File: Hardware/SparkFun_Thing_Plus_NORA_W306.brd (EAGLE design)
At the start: 22.9 x 58.4 mm, 153 parts, among them J1 THING_PLUS_LOGICAL, J2 LiPo, J3 QWIIC_RA, J4 MICRO-SDFRICTION, J5 USB-C, J6 SWD (DNP), Q1 3.1A/30V/105mΩ, Q2 MBT3904DW1T1, U1 UBLOX_NORA_W306, U3 XC6222B331MR-G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

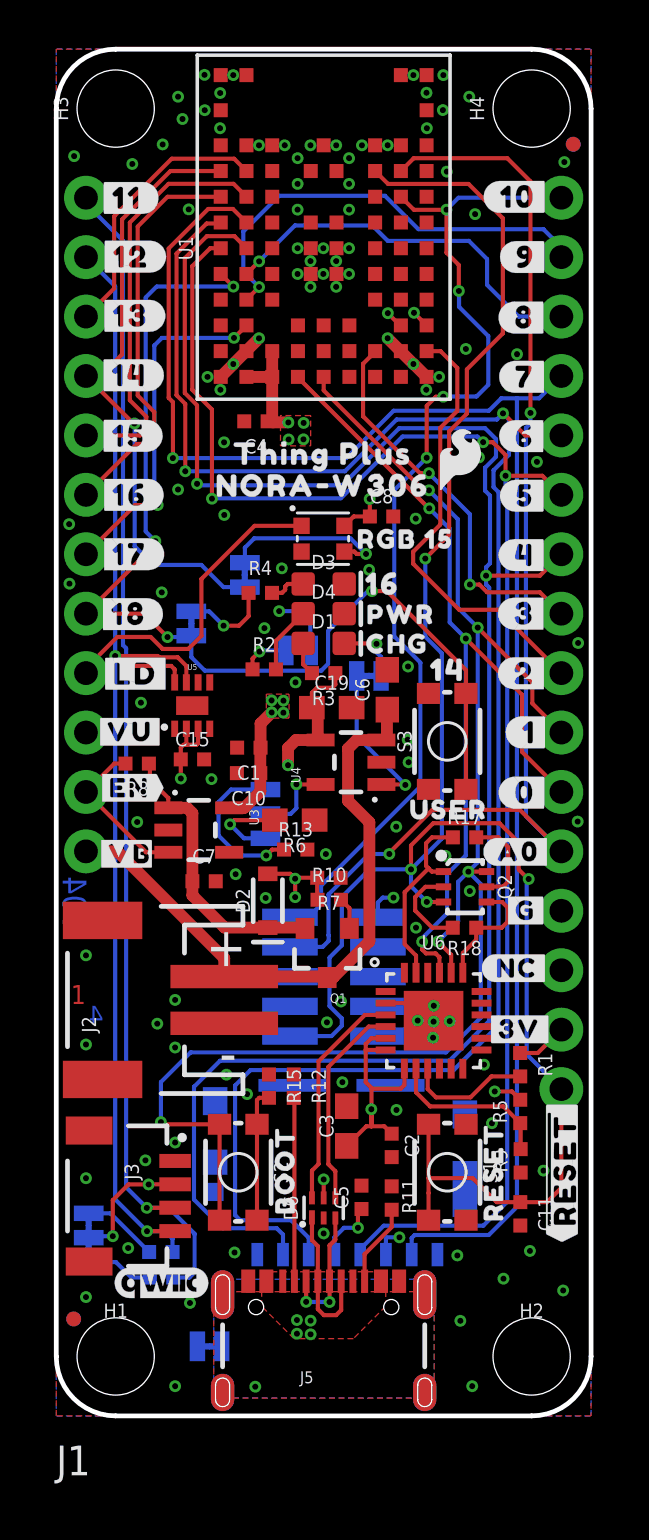
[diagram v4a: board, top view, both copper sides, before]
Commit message: Corrected User button and STAT LED silk
-Moved button to Arduino "17"
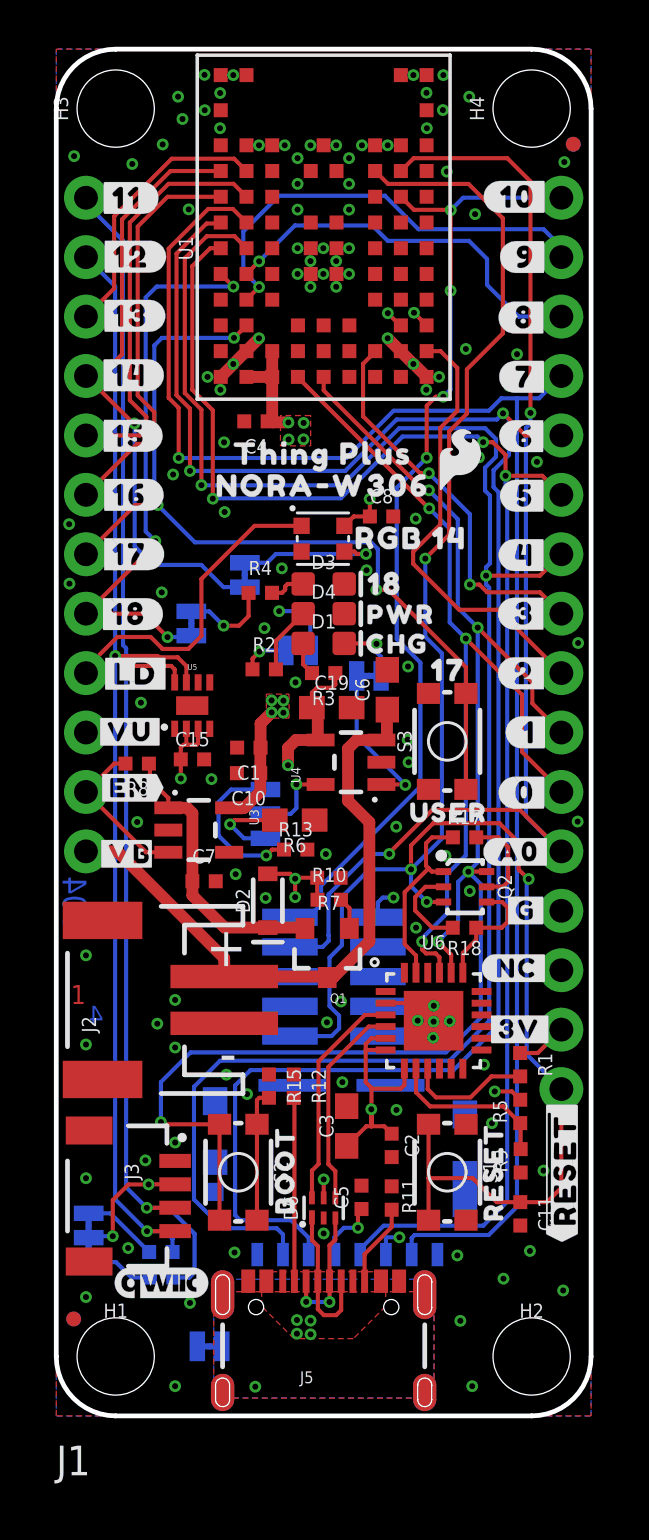
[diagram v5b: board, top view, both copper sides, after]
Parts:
- removed U$25: (no value), output:16165
- removed U$34: (no value), output:1417
- removed U$73: (no value), output:RGB_155
- added U$21: (no value), output:1830
- added U$22: (no value), output:1714141833
- added U$24: (no value), output:RGB_14141832
- moved U$7 0.13 mm to (16.8, 25.8)
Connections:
- net PB22: no longer S3.1, S3.2
- net PB23: now also S3.1, S3.2
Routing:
- net PB23: track 15.1 -> 37.5 mm, vias 2 -> 3
- net PB22: track 46.2 -> 24.6 mm, vias 4 -> 3
- net PA27/SWD_DATA: track 44.2 -> 41.9 mm
- net N$10: track 7.23 -> 6.30 mm

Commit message: rerouting some stuff
-Re-routed SPI lined to removed one via in SPI0_CLK net
-Nudged some stuff to create a bit more clearance between RX/TX log and SPI traces on long north-south journey.
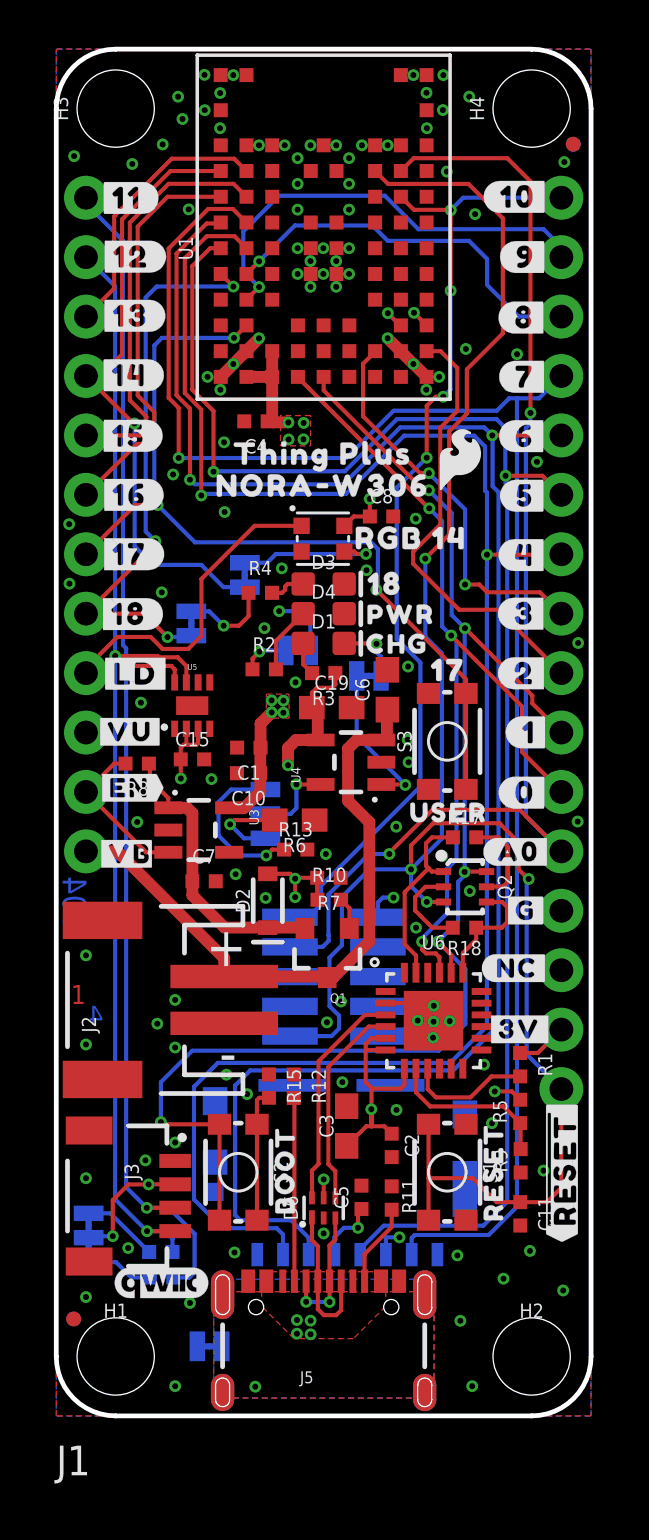
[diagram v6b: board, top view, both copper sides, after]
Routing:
- net PA7/UART-LOG-TXD: track 65.6 -> 62.3 mm
- net PB18/SPI0_PICO: track 78.0 -> 76.9 mm
- net PB21/SPI0_CS: track 79.8 -> 78.8 mm
- net PB20/SPI0_CLK: track 67.8 -> 67.4 mm, vias 3 -> 2
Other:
- board text added: "Soldermask: Red Thickness: 1.6mm Four Layer Design 1oz copper outer 0.5oz copper inner Finish: HASL Stackup: JLC7628 Material: TG155"
- board text removed: "Board thickness is 1.6mm 4-Layer 1oz copper outer 0.5oz copper inner Surface Finish: HASL"

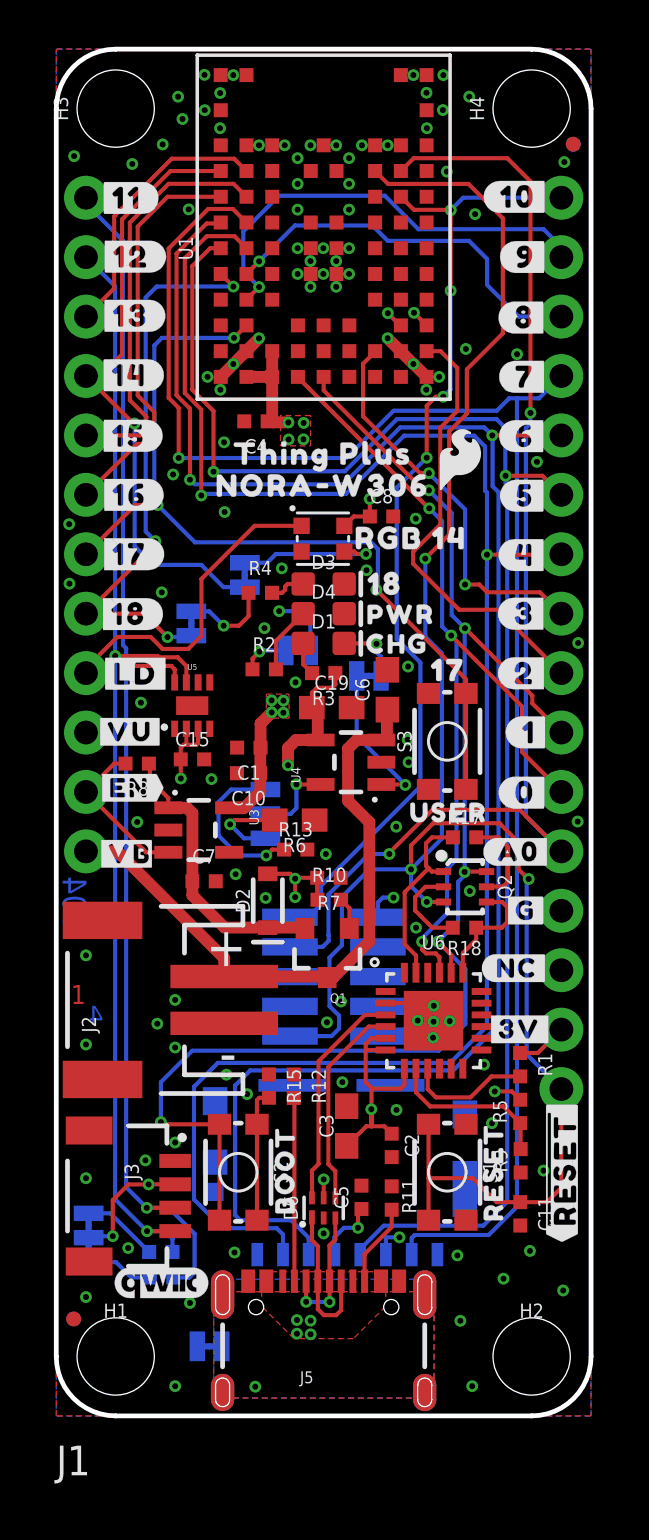
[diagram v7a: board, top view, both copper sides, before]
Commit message: Added V-MEAS jumper
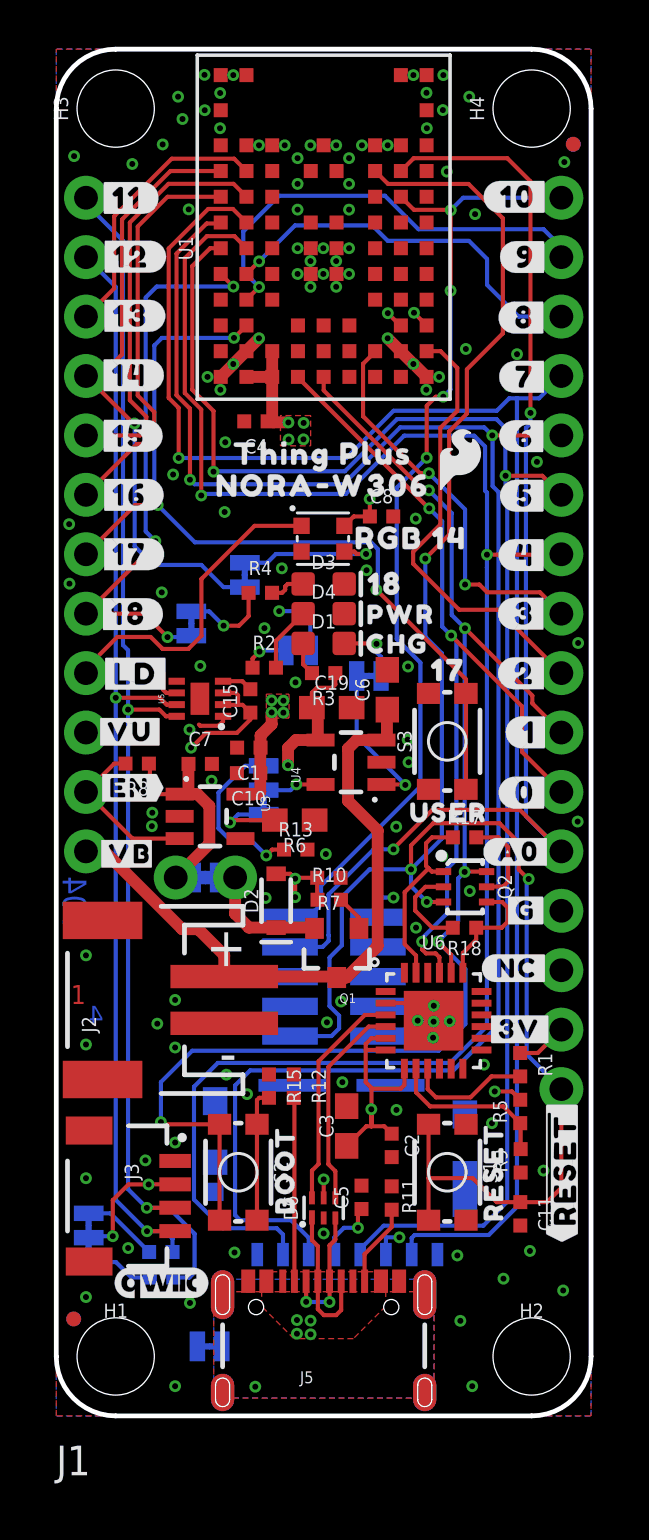
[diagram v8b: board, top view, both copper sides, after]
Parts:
- removed U$42: (no value), output:#VBAT#0
- added MEAS: (no value), SparkFun-Jumpers:COMBO-JUMPER_2_NC_TRACE
- added U$25: (no value), output:#MEAS#1714141834
- added U$26: (no value), output:#VB26
- moved U$60 7.72 mm to (15.9, 18.8)
- moved C7 5.02 mm to (6.15, 27.9)
- moved C15 3.52 mm to (8.30, 30.6), turned to 90 degrees
- moved LOGO3 2.73 mm to (1.82, 16.0), turned to 90 degrees
- moved U$4 1.29 mm to (9.63, 29.0)
- moved U$9 1.23 mm to (9.57, 24.5)
- moved CUR 1.02 mm to (8.86, 26.7)
- moved U$3 0.92 mm to (11.7, 26.6)
- moved U$11 0.89 mm to (10.8, 26.7)
- moved U3 0.76 mm to (6.57, 25.6)
- moved U5 0.44 mm to (6.14, 30.7), turned to 90 degrees
- moved Q1 0.41 mm to (12.0, 19.8)
- moved D2 0.36 mm to (9.40, 22.0)
- moved R2 0.07 mm to (8.89, 32.0)
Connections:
- new net N$23: D2.C, MEAS.1, MEAS.3, Q1.2
- net VIN: now also MEAS.2, MEAS.4; no longer D2.C, Q1.2
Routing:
- net N$23: track 0.00 -> 5.96 mm
- net GND: track 7.53 -> 11.5 mm, vias 117 -> 118
- net V_BATT: track 35.9 -> 39.9 mm
- net VIN: track 12.3 -> 9.55 mm
- net PA25/SCL: track 64.7 -> 63.5 mm
- net N$9: track 3.48 -> 2.54 mm
- net 3.3V: track 47.0 -> 46.3 mm
- net PA26/SDA: track 71.2 -> 70.6 mm
